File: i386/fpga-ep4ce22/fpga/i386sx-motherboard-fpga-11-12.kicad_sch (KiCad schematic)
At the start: 1 part, among them U3 (5/6) EP4CE22F17C8N

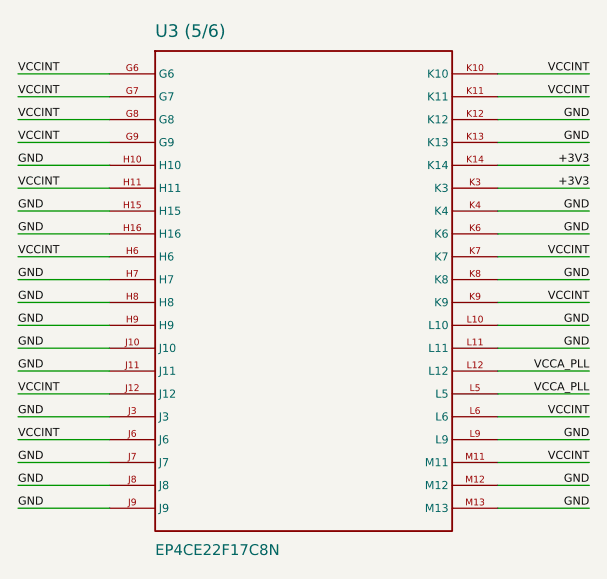
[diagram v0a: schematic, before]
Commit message: Publish the motherboards' KiCad files
From socket3@c0f6464 socket7@9205469 socket370@524f5b1 i386@bea926c
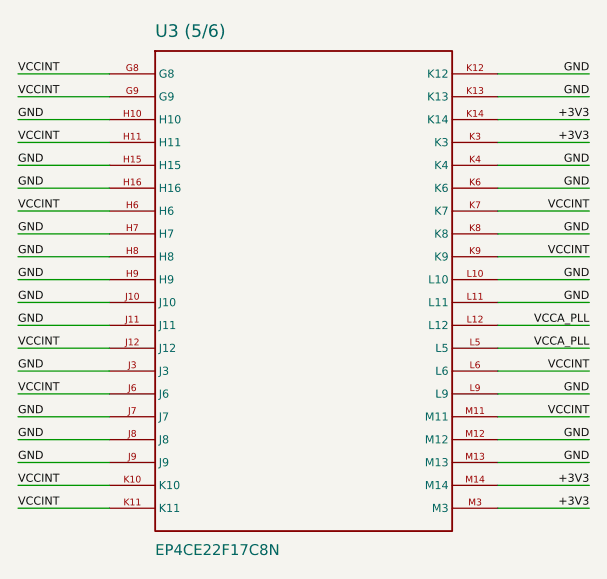
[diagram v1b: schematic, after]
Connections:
- net +3V3: now also U3 (5/6).M14, U3 (5/6).M3
- net VCCINT: no longer U3 (5/6).G6, U3 (5/6).G7
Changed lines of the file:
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@@
     (property "Reference" "U3 (5/6)" (at 44.46 17.65 0) (effects (font (size 1.4 1.4)) (justify left bottom)))
     (property "Value" "EP4CE22F17C8N" (at 44.46 73.79 0) (effects (font (size 1.2 1.2)) (justify left top)))
-    (instances (project "i386sx-motherboard" (path "/0ac398a9-1d89-4090-a36f-db7b4d3d6c0d/1bf7dfe8-13a7-4ad3-928e-1a6afede25a4" (reference "U3") (unit 1))))
+    (instances (project "i386sx-motherboard" (path "/ea05416d-ce24-4c39-9113-85b33d9a88b0/8ca95ab3-f3bc-4e68-b49c-5a6099263be1" (reference "U3") (unit 1))))
   )
   (wire (pts (xy 39.38 21.59) (xy 29.22 21.59)) (stroke (width 0) (type default)))
@@
   (label "VCCINT" (at 29.22 21.59 0) (effects (font (size 0.9 0.9)) (justify left bottom)))
   (label "VCCINT" (at 29.22 24.13 0) (effects (font (size 0.9 0.9)) (justify left bottom)))
-  (label "VCCINT" (at 29.22 26.67 0) (effects (font (size 0.9 0.9)) (justify left bottom)))
   (label "VCCINT" (at 29.22 29.21 0) (effects (font (size 0.9 0.9)) (justify left bottom)))
-  (label "VCCINT" (at 29.22 34.29 0) (effects (font (size 0.9 0.9)) (justify left bottom)))
-  (label "VCCINT" (at 29.22 41.91 0) (effects (font (size 0.9 0.9)) (justify left bottom)))
+  (label "VCCINT" (at 29.22 36.83 0) (effects (font (size 0.9 0.9)) (justify left bottom)))
+  (label "VCCINT" (at 29.22 52.07 0) (effects (font (size 0.9 0.9)) (justify left bottom)))
   (label "VCCINT" (at 29.22 57.15 0) (effects (font (size 0.9 0.9)) (justify left bottom)))
-  (label "VCCINT" (at 29.22 62.23 0) (effects (font (size 0.9 0.9)) (justify left bottom)))
-  (label "VCCINT" (at 92.70 21.59 0) (effects (font (size 0.9 0.9)) (justify right bottom)))
-  (label "VCCINT" (at 92.70 24.13 0) (effects (font (size 0.9 0.9)) (justify right bottom)))
+  (label "VCCINT" (at 29.22 67.31 0) (effects (font (size 0.9 0.9)) (justify left bottom)))
+  (label "VCCINT" (at 29.22 69.85 0) (effects (font (size 0.9 0.9)) (justify left bottom)))
+  (label "VCCINT" (at 92.70 36.83 0) (effects (font (size 0.9 0.9)) (justify right bottom)))
   (label "VCCINT" (at 92.70 41.91 0) (effects (font (size 0.9 0.9)) (justify right bottom)))
-  (label "VCCINT" (at 92.70 46.99 0) (effects (font (size 0.9 0.9)) (justify right bottom)))
+  (label "VCCINT" (at 92.70 54.61 0) (effects (font (size 0.9 0.9)) (justify right bottom)))
   (label "VCCINT" (at 92.70 59.69 0) (effects (font (size 0.9 0.9)) (justify right bottom)))
-  (label "VCCINT" (at 92.70 64.77 0) (effects (font (size 0.9 0.9)) (justify right bottom)))
+  (label "GND" (at 29.22 26.67 0) (effects (font (size 0.9 0.9)) (justify left bottom)))
   (label "GND" (at 29.22 31.75 0) (effects (font (size 0.9 0.9)) (justify left bottom)))
-  (label "GND" (at 29.22 36.83 0) (effects (font (size 0.9 0.9)) (justify left bottom)))
+  (label "GND" (at 29.22 34.29 0) (effects (font (size 0.9 0.9)) (justify left bottom)))
   (label "GND" (at 29.22 39.37 0) (effects (font (size 0.9 0.9)) (justify left bottom)))
+  (label "GND" (at 29.22 41.91 0) (effects (font (size 0.9 0.9)) (justify left bottom)))
   (label "GND" (at 29.22 44.45 0) (effects (font (size 0.9 0.9)) (justify left bottom)))
   (label "GND" (at 29.22 46.99 0) (effects (font (size 0.9 0.9)) (justify left bottom)))
   (label "GND" (at 29.22 49.53 0) (effects (font (size 0.9 0.9)) (justify left bottom)))
-  (label "GND" (at 29.22 52.07 0) (effects (font (size 0.9 0.9)) (justify left bottom)))
   (label "GND" (at 29.22 54.61 0) (effects (font (size 0.9 0.9)) (justify left bottom)))
   (label "GND" (at 29.22 59.69 0) (effects (font (size 0.9 0.9)) (justify left bottom)))
+  (label "GND" (at 29.22 62.23 0) (effects (font (size 0.9 0.9)) (justify left bottom)))
   (label "GND" (at 29.22 64.77 0) (effects (font (size 0.9 0.9)) (justify left bottom)))
-  (label "GND" (at 29.22 67.31 0) (effects (font (size 0.9 0.9)) (justify left bottom)))
-  (label "GND" (at 29.22 69.85 0) (effects (font (size 0.9 0.9)) (justify left bottom)))
-  (label "GND" (at 92.70 26.67 0) (effects (font (size 0.9 0.9)) (justify right bottom)))
-  (label "GND" (at 92.70 29.21 0) (effects (font (size 0.9 0.9)) (justify right bottom)))
-  (label "GND" (at 92.70 36.83 0) (effects (font (size 0.9 0.9)) (justify right bottom)))
+  (label "GND" (at 92.70 21.59 0) (effects (font (size 0.9 0.9)) (justify right bottom)))
+  (label "GND" (at 92.70 24.13 0) (effects (font (size 0.9 0.9)) (justify right bottom)))
+  (label "GND" (at 92.70 31.75 0) (effects (font (size 0.9 0.9)) (justify right bottom)))
+  (label "GND" (at 92.70 34.29 0) (effects (font (size 0.9 0.9)) (justify right bottom)))
   (label "GND" (at 92.70 39.37 0) (effects (font (size 0.9 0.9)) (justify right bottom)))
   (label "GND" (at 92.70 44.45 0) (effects (font (size 0.9 0.9)) (justify right bottom)))
-  (label "GND" (at 92.70 49.53 0) (effects (font (size 0.9 0.9)) (justify right bottom)))
-  (label "GND" (at 92.70 52.07 0) (effects (font (size 0.9 0.9)) (justify right bottom)))
+  (label "GND" (at 92.70 46.99 0) (effects (font (size 0.9 0.9)) (justify right bottom)))
+  (label "GND" (at 92.70 57.15 0) (effects (font (size 0.9 0.9)) (justify right bottom)))
   (label "GND" (at 92.70 62.23 0) (effects (font (size 0.9 0.9)) (justify right bottom)))
-  (label "GND" (at 92.70 67.31 0) (effects (font (size 0.9 0.9)) (justify right bottom)))
-  (label "GND" (at 92.70 69.85 0) (effects (font (size 0.9 0.9)) (justify right bottom)))
-  (label "+3V3" (at 92.70 31.75 0) (effects (font (size 0.9 0.9)) (justify right bottom)))
-  (label "+3V3" (at 92.70 34.29 0) (effects (font (size 0.9 0.9)) (justify right bottom)))
-  (label "VCCA_PLL" (at 92.70 54.61 0) (effects (font (size 0.9 0.9)) (justify right bottom)))
-  (label "VCCA_PLL" (at 92.70 57.15 0) (effects (font (size 0.9 0.9)) (justify right bottom)))
+  (label "GND" (at 92.70 64.77 0) (effects (font (size 0.9 0.9)) (justify right bottom)))
+  (label "+3V3" (at 92.70 26.67 0) (effects (font (size 0.9 0.9)) (justify right bottom)))
+  (label "+3V3" (at 92.70 29.21 0) (effects (font (size 0.9 0.9)) (justify right bottom)))
+  (label "+3V3" (at 92.70 67.31 0) (effects (font (size 0.9 0.9)) (justify right bottom)))
+  (label "+3V3" (at 92.70 69.85 0) (effects (font (size 0.9 0.9)) (justify right bottom)))
+  (label "VCCA_PLL" (at 92.70 49.53 0) (effects (font (size 0.9 0.9)) (justify right bottom)))
+  (label "VCCA_PLL" (at 92.70 52.07 0) (effects (font (size 0.9 0.9)) (justify right bottom)))
 )
